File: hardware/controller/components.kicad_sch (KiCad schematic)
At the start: 17 parts, among them U5 AP2112K-3.3, U6 SN74LVC1T45DBV

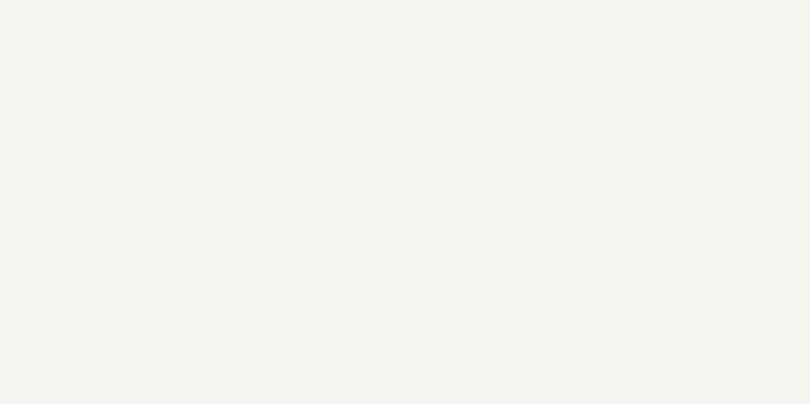
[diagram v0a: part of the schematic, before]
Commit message: use different socket for data vs power to avoid accidents
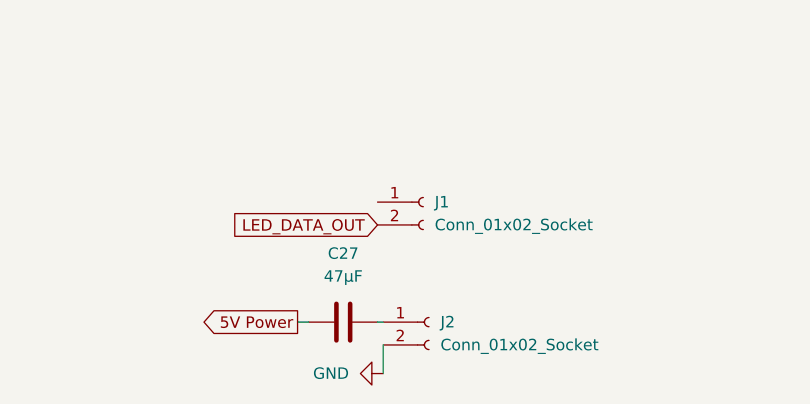
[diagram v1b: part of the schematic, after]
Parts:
- added C27: 47µF, Capacitor_SMD:C_1206_3216Metric, symbol Device:C
- added J1, J2: Conn_01x02_Socket, footprints:CONN-SMD_ZX-XH2.54-2PLT, symbol Connector:Conn_01x02_Socket
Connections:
- net 5V Power: now also C27.1
- net GND: now also J2.2 (Pin_2)
- new net: C27.2, J2.1 (Pin_1)
- new net LED_DATA_OUT: J1.2 (Pin_2)

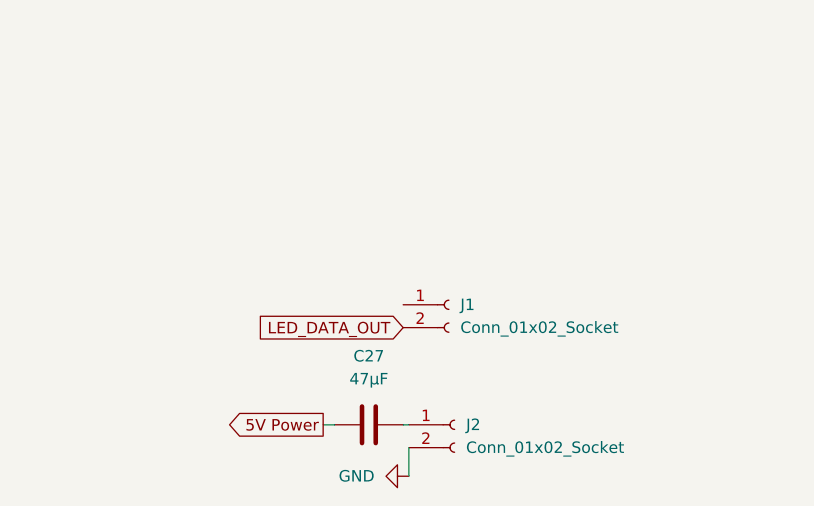
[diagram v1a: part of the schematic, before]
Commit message: remove unnecessary test pad and add silkscreen for sockets
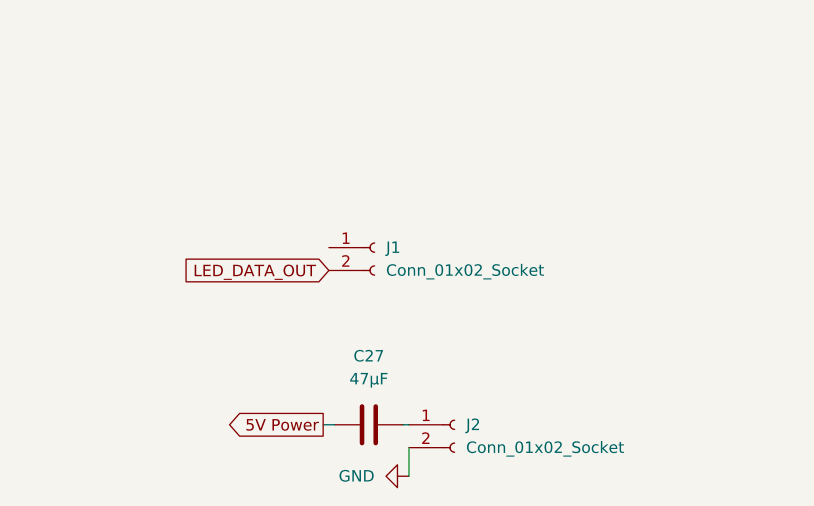
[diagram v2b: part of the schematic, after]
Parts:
- J1: footprint footprints:CONN-SMD_ZX-XH2.54-2PLT -> footprints:CONN-SMD_B2B-PH-SM4-TBT-LF-SN; JLCPCB Part # C7429680 -> C265003
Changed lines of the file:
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@@
 		)
 	)
+	(global_label "LED_DATA_OUT"
+		(shape input)
+		(at 52.07 153.67 180)
+		(fields_autoplaced yes)
+		(effects
+			(font
+				(size 1.27 1.27)
+			)
+			(justify right)
+		)
+		(property "Intersheetrefs" "${INTERSHEET_REFS}"
+			(at 35.6591 153.67 0)
+			(hide yes)
+			(show_name no)
+			(do_not_autoplace no)
+			(effects
+				(font
+					(size 1.27 1.27)
+				)
+				(justify right)
+			)
+		)
+	)
 	(global_label "LED DATA"
 		(shape input)
@@
 		)
 	)
-	(global_label "LED_DATA_OUT"
-		(shape input)
-		(at 60.325 160.02 180)
-		(fields_autoplaced yes)
-		(effects
-			(font
-				(size 1.27 1.27)
-			)
-			(justify right)
-		)
-		(property "Intersheetrefs" "${INTERSHEET_REFS}"
-			(at 43.9141 160.02 0)
-			(hide yes)
-			(show_name no)
-			(do_not_autoplace no)
-			(effects
-				(font
-					(size 1.27 1.27)
-				)
-				(justify right)
-			)
-		)
-	)
 	(global_label "USB Data -"
 		(shape output)
@@
 	)
 	(symbol
-		(lib_id "Connector:Conn_01x02_Socket")
-		(at 65.405 157.48 0)
+		(lib_id "power:GND")
+		(at 55.88 115.57 0)
 		(unit 1)
 		(body_style 1)
@@
 		(dnp no)
 		(fields_autoplaced yes)
-		(property "Reference" "J1"
-			(at 66.675 157.4799 0)
+		(property "Reference" "#PWR029"
+			(at 55.88 121.92 0)
+			(hide yes)
 			(show_name no)
 			(do_not_autoplace no)
@@
 					(size 1.27 1.27)
 				)
-				(justify left)
 			)
 		)
-		(property "Value" "Conn_01x02_Socket"
-			(at 66.675 160.0199 0)
+		(property "Value" "GND"
+			(at 55.88 120.65 0)
 			(show_name no)
 			(do_not_autoplace no)
@@
 					(size 1.27 1.27)
 				)
-				(justify left)
 			)
 		)
-		(property "Footprint" "footprints:CONN-SMD_ZX-XH2.54-2PLT"
-			(at 65.405 157.48 0)
+		(property "Footprint" ""
+			(at 55.88 115.57 0)
 			(hide yes)
 			(show_name no)
@@
 		)
 		(property "Datasheet" ""
-			(at 65.405 157.48 0)
-			(hide yes)
-			(show_name no)
-			(do_not_autoplace no)
-			(effects
-				(font
-					(size 1.27 1.27)
-				)
-			)
-		)
-		(property "Description" "Generic connector, single row, 01x02, script generated"
-			(at 65.405 157.48 0)
+			(at 55.88 115.57 0)
 			(hide yes)
 			(show_name no)
@@
 			)
 		)
-		(property "JLCPCB Part #" "C7429680"
-			(at 65.405 157.48 0)
+		(property "Description" "Power symbol creates a global label with name \"GND\" , ground"
+			(at 55.88 115.57 0)
 			(hide yes)
 			(show_name no)
@@
 			)
 		)
-		(pin "2"
-		)
 		(pin "1"
 		)
@@
 			(project "controller"
 				(path "/d7bd6c74-3e25-4440-9b6a-904f2e2d9596"
-					(reference "J1")
+					(reference "#PWR029")
 					(unit 1)
 				)
@@
 	)
 	(symbol
-		(lib_id "power:GND")
-		(at 55.88 115.57 0)
+		(lib_id "Device:R")
+		(at 55.88 111.76 180)
 		(unit 1)
 		(body_style 1)
@@
 		(dnp no)
 		(fields_autoplaced yes)
-		(property "Reference" "#PWR029"
-			(at 55.88 121.92 0)
-			(hide yes)
+		(property "Reference" "R15"
+			(at 58.42 110.4899 0)
 			(show_name no)
 			(do_not_autoplace no)
@@
 					(size 1.27 1.27)
 				)
+				(justify right)
 			)
 		)
-		(property "Value" "GND"
-			(at 55.88 120.65 0)
+		(property "Value" "100kΩ"
+			(at 58.42 113.0299 0)
 			(show_name no)
 			(do_not_autoplace no)
@@
 					(size 1.27 1.27)
 				)
+				(justify right)
 			)
 		)
-		(property "Footprint" ""
-			(at 55.88 115.57 0)
+		(property "Footprint" "Resistor_SMD:R_0603_1608Metric"
+			(at 57.658 111.76 90)
 			(hide yes)
 			(show_name no)
@@
 			)
 		)
-		(property "Datasheet" ""
-			(at 55.88 115.57 0)
+		(property "Datasheet" "https://jlcpcb.com/api/file/downloadByFileSystemAccessId/8579706350726930432"
+			(at 55.88 111.76 0)
 			(hide yes)
 			(show_name no)
@@
 			)
 		)
-		(property "Description" "Power symbol creates a global label with name \"GND\" , ground"
-			(at 55.88 115.57 0)
+		(property "Description" "Resistor"
+			(at 55.88 111.76 0)
+			(hide yes)
+			(show_name no)
+			(do_not_autoplace no)
+			(effects
+				(font
+					(size 1.27 1.27)
+				)
+			)
+		)
+		(property "JLCPCB Part #" "C25803"
+			(at 55.88 111.76 90)
 			(hide yes)
 			(show_name no)
@@
 		(pin "1"
 		)
+		(pin "2"
+		)
 		(instances
 			(project "controller"
 				(path "/d7bd6c74-3e25-4440-9b6a-904f2e2d9596"
-					(reference "#PWR029")
+					(reference "R15")
 					(unit 1)
 				)
@@
 	)
 	(symbol
-		(lib_id "Device:R")
-		(at 55.88 111.76 180)
+		(lib_id "Connector:Conn_01x02_Socket")
+		(at 57.15 151.13 0)
 		(unit 1)
 		(body_style 1)
@@
 		(dnp no)
 		(fields_autoplaced yes)
-		(property "Reference" "R15"
-			(at 58.42 110.4899 0)
+		(property "Reference" "J1"
+			(at 58.42 151.1299 0)
 			(show_name no)
 			(do_not_autoplace no)
@@
 					(size 1.27 1.27)
 				)
-				(justify right)
+				(justify left)
 			)
 		)
-		(property "Value" "100kΩ"
-			(at 58.42 113.0299 0)
+		(property "Value" "Conn_01x02_Socket"
+			(at 58.42 153.6699 0)
 			(show_name no)
 			(do_not_autoplace no)
@@
 					(size 1.27 1.27)
 				)
-				(justify right)
+				(justify left)
 			)
 		)
-		(property "Footprint" "Resistor_SMD:R_0603_1608Metric"
-			(at 57.658 111.76 90)
+		(property "Footprint" "footprints:CONN-SMD_B2B-PH-SM4-TBT-LF-SN"
+			(at 57.15 151.13 0)
 			(hide yes)
 			(show_name no)
@@
 			)
 		)
-		(property "Datasheet" "https://jlcpcb.com/api/file/downloadByFileSystemAccessId/8579706350726930432"
-			(at 55.88 111.76 0)
+		(property "Datasheet" "https://jlc-prod-smt.oss-eu-central-1.aliyuncs.com/smtDataManualFile/8588902703158607872-C265003.pdf?response-content-disposition=attachment%3B%20filename%3DC265003.pdf%3B%20filename%2A%3DUTF-8%27%27C265003.pdf&x-oss-date=20260530T184618Z&x-oss-expires=1800&x-oss-security-token=CAISgAN1q6Ft5B2yfSjIr5mMGOPH2b5C56u6RmrwoVgfesNa3pGdrjz2IHhMdHJsAOodtv0%2FmmhT6PkclqRLcbhpcmfjV%2BZHzLB8qYMJrTZO4J7b16cNrbH4M4H6aXeirtuwDsz9SNTCALjPD3nPii50x5bjaDymRCbLGJaViJlhHLN1Ow6jdmhpCctxLAlvo9NgFxm3D%2Fu2NQPwiWf9FVdhvhEG6Vly8qOi2MaRmFy8yFTx0b0SvJ%2BjYMrmPctoN9JnSdC5mfdzau3a1TJ84gRD0a5wkaVA1zbDs5bfISEIuUzebreLqY03dV4mOvdqIcMe8qigz88fk%2FfIioH6xyxKOexoSCnFTOiiupCcQLPyao9jLu6iayqViY7QaIOTqQohZmkAMwVOasAsI3Ngh4zF97Qt0cVNkXO9gWfLI8DtuMleWorMUcNC5tHD0eS19jklBdzSlusJRAJJUVBflCeKEaRNSAd3WGhEfM2%2BBt4QT30w5N2u00S8OSMIj6WwtaKWD5sagAEiB9a8Fe3Xz48X2tP6dxg54Vro9nibq7GRPtzBohN8u1QdmxofnrAafgnnqWIAyQYzEZD7Qmyn521BE9LOYbykf0HEMcjUKnha5PhgCA%2BaTkV%2BbWuE1SITzT9cI0CaBUqZ3vKId6FEL2fcnTSF0BDC6iF%2Bhf1ATGD2uciyP2xLKSAA&x-oss-signature-version=OSS4-HMAC-SHA256&x-oss-credential=STS.NZ9SYs4acPiQDLAEXJvLv1T6L%2F20260530%2Feu-central-1%2Foss%2Faliyun_v4_request&x-oss-signature=9be76bdf4ed042f2478c7de920dfc88ba2fe608f5eef2b87c8aebd4d72e4c4dc"
+			(at 57.15 151.13 0)
 			(hide yes)
 			(show_name no)
@@
 			)
 		)
-		(property "Description" "Resistor"
-			(at 55.88 111.76 0)
+		(property "Description" "Generic connector, single row, 01x02, script generated"
+			(at 57.15 151.13 0)
 			(hide yes)
 			(show_name no)
@@
 			)
 		)
-		(property "JLCPCB Part #" "C25803"
-			(at 55.88 111.76 90)
+		(property "JLCPCB Part #" "C265003"
+			(at 57.15 151.13 0)
 			(hide yes)
 			(show_name no)
@@
 			)
 		)
-		(pin "1"
-		)
 		(pin "2"
 		)
+		(pin "1"
+		)
 		(instances
 			(project "controller"
 				(path "/d7bd6c74-3e25-4440-9b6a-904f2e2d9596"
-					(reference "R15")
+					(reference "J1")
 					(unit 1)
 				)

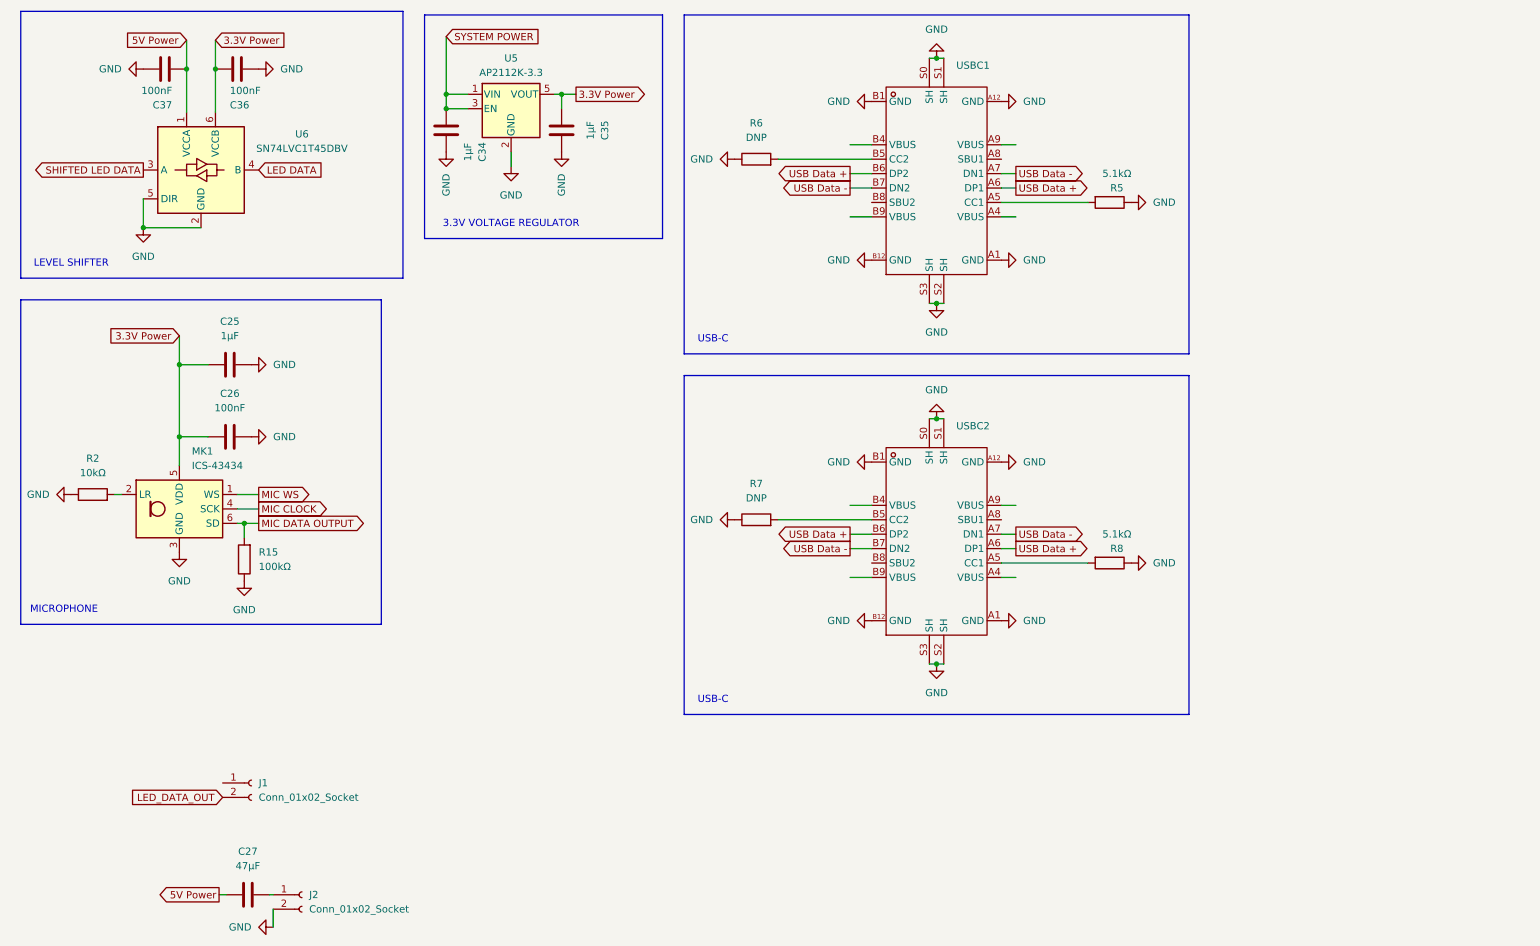
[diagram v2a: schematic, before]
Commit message: remove old usb from controller
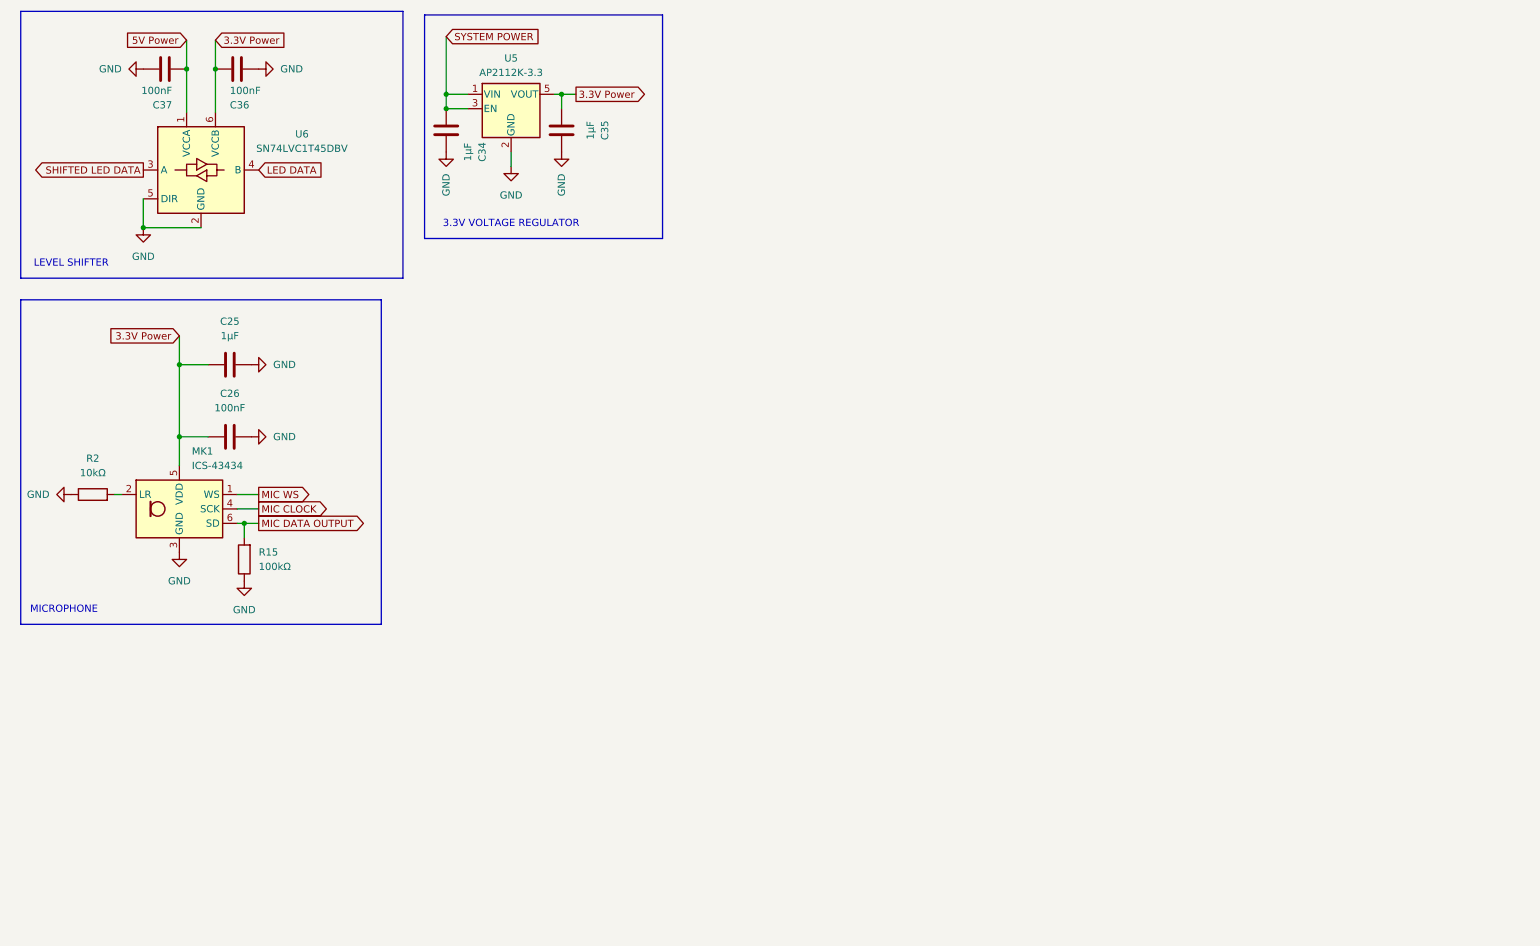
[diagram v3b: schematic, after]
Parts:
- removed C27: 47µF, Capacitor_SMD:C_1206_3216Metric, symbol Device:C
- removed J1: Conn_01x02_Socket, footprints:CONN-SMD_B2B-PH-SM4-TBT-LF-SN, symbol Connector:Conn_01x02_Socket
- removed J2: Conn_01x02_Socket, footprints:CONN-SMD_ZX-XH2.54-2PLT, symbol Connector:Conn_01x02_Socket
- removed R5, R8: 5.1kΩ, Resistor_SMD:R_0603_1608Metric, symbol Device:R
- removed R6, R7: DNP, Resistor_SMD:R_0603_1608Metric, symbol Device:R
- removed USBC1, USBC2: (no value), footprints:USB-C_SMD-TYPE-C-31-M-12, symbol USB_C:TYPE-C-31-M-12
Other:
- note removed: "USB-C"
